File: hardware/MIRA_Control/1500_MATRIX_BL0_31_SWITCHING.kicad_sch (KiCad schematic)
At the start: 164 parts, among them U1500 ADG5412, U1501 ADG5412, U1502 ADG5412, U1503 ADG5412, U1504 ADG5412, U1505 ADG5412, U1506 ADG5412, U1507 ADG5412, U1508 ADG5412, U1509 ADG5412, U1510 ADG5412, U1511 ADG5412, U1512 ADG5412, U1513 ADG5412, U1514 ADG5412, U1515 ADG5412, U1516 ADG5408, U1517 ADG5408, U1518 ADG5408, U1519 ADG5408

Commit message: Protect unpowered signal domains and qualify local supplies; retain startup and fault interlocks
MIRA-Startup-Patch: 7ffae17756ebcf923eff1212bb1aade8fbdfae03a9ca8ecebc69d3da3d3b4ba2
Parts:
- U1500, U1501, U1502, U1503, U1504, U1505, U1506, U1507, U1508, U1509, U1510, U1511, U1512, U1513, U1514, U1515: value ADG5412 -> TMUX7212PWR; symbol MIRA_RevA:ADG5412_MIRA_MAT -> MIRA_RevA:TMUX7212PWR_SIGNAL_MIRA; MPN ADG5412BRUZ -> TMUX7212PWR; Manufacturer Analog Devices -> Texas Instruments
- U1516, U1517, U1518, U1519: value ADG5408 -> TMUX7208PWR; symbol MIRA_RevA:ADG5408_MIRA_MAT -> MIRA_RevA:TMUX7208PWR_SIGNAL_MIRA; MPN ADG5408BRUZ -> TMUX7208PWR; Manufacturer Analog Devices -> Texas Instruments

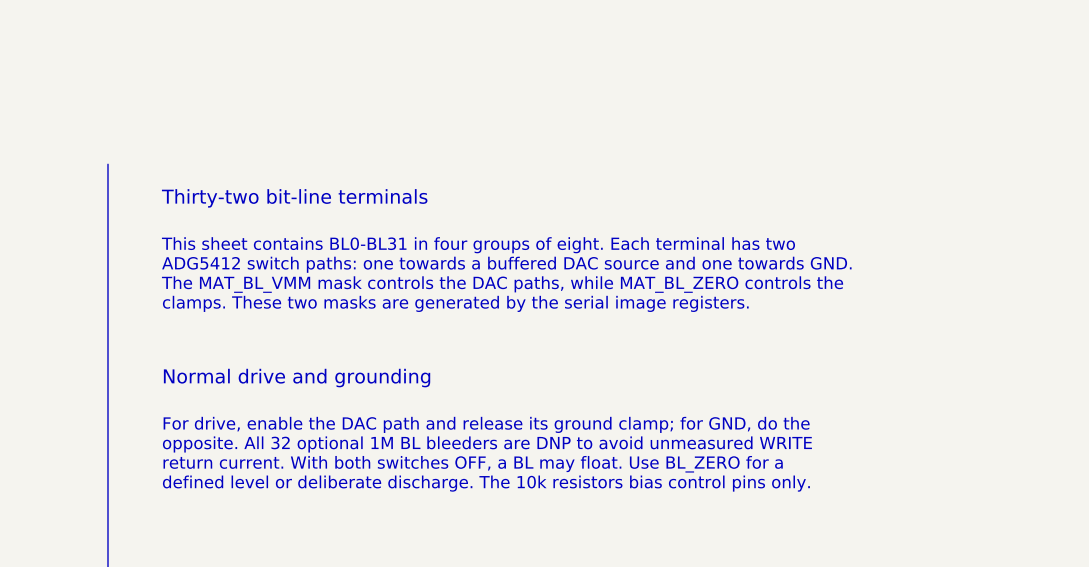
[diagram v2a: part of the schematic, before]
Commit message: MIRA.05: analog requirements and schematic fixes
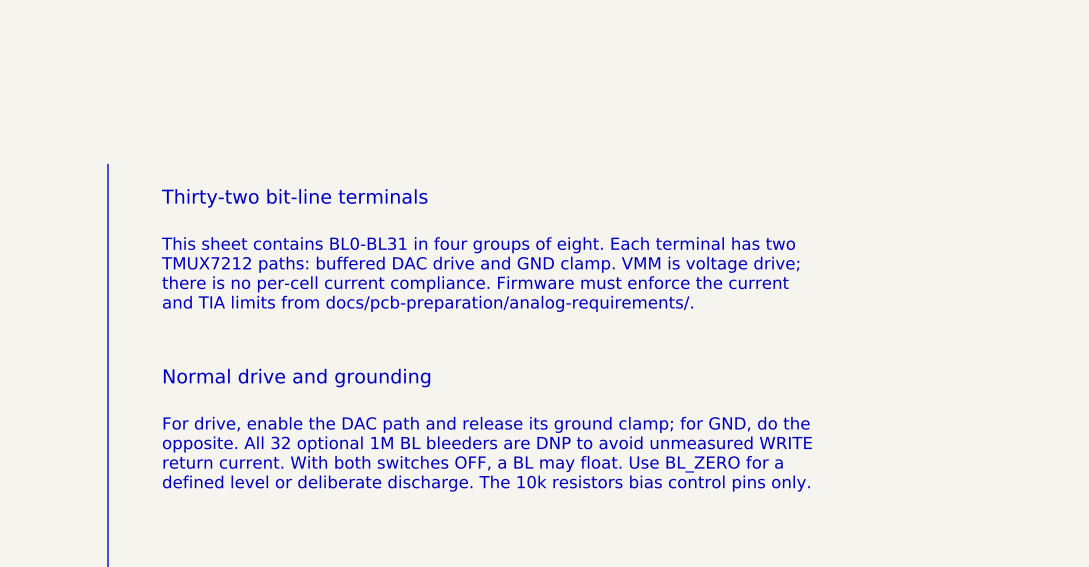
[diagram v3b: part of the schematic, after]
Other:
- note added: "This sheet contains BL0-BL31 in four groups of eight. Each terminal has two TMUX7212 paths: buffered DAC drive and GND clamp. VMM is voltage drive; there is no per-cell current compliance. Firmware must enforce the current and TIA limits from docs/pcb-preparation/analog-requirements/."
- note removed: "This sheet contains BL0-BL31 in four groups of eight. Each terminal has two ADG5412 switch paths: one towards a buffered DAC source and one towards GND. The MAT_BL_VMM mask controls the DAC paths, while MAT_BL_ZERO controls the clamps. These two masks are generated by the serial image registers."
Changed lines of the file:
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@@
 		)
 	)
-	(text "This sheet contains BL0-BL31 in four groups of eight. Each terminal has two\nADG5412 switch paths: one towards a buffered DAC source and one towards GND.\nThe MAT_BL_VMM mask controls the DAC paths, while MAT_BL_ZERO controls the\nclamps. These two masks are generated by the serial image registers."
-		(exclude_from_sim no)
-		(at 315 42.34 0)
-		(effects
-			(font
-				(size 1.35 1.35)
-				(color 0 70 160 1)
-			)
-			(justify left top)
-		)
-	)
+	(text "This sheet contains BL0-BL31 in four groups of eight. Each terminal has two\nTMUX7212 paths: buffered DAC drive and GND clamp. VMM is voltage drive;\nthere is no per-cell current compliance. Firmware must enforce the current\nand TIA limits from docs/pcb-preparation/analog-requirements/." (exclude_from_sim no) (at 315 42.34 0) (effects (font (size 1.35 1.35) (color 0 70 160 1)) (justify left top)))
 	(text "BL8 / DAC + GND"
 		(exclude_from_sim no)

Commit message: Review MIRA.06 components, connectors and assembly
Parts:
- C1500, C1501, C1502, C1503, C1504, C1505, C1506, C1507, C1508, C1509, C1510, C1511, C1512, C1513, C1514, C1515, C1516, C1517, C1518, C1519, C1520, C1521, C1522, C1523, C1524, C1526, C1527, C1529, C1530, C1532, C1533, C1534, C1535, C1536, C1537, C1538, C1539, C1540, C1541, C1543: MPN (none) -> CC0603KRX7R9BB104; Manufacturer Murata -> YAGEO
- C1525, C1528, C1531, C1542: MPN (none) -> CC0603KRX7R9BB105; Manufacturer Murata -> YAGEO
